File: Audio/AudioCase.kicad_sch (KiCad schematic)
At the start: 3 parts, among them J1 PD給電, J2 入力ジャック, J3 出力ジャック

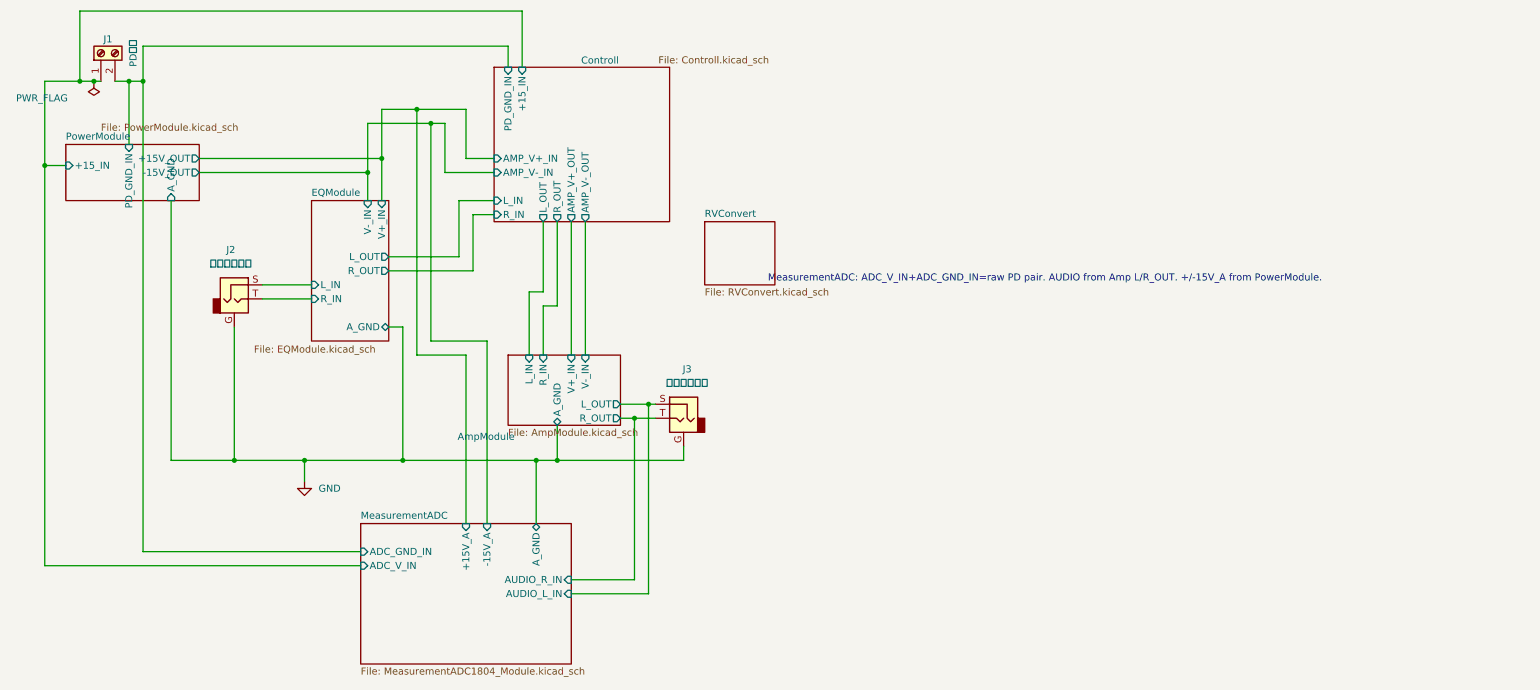
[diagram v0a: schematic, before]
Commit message: Add AdcBuffer unity-gain sheet between Amp and MeasurementADC.
Inserts AdcBufferModule (NE5532/OPA1652 DIP followers, 100k bias, 47Ω
series, 0.1µF decouple) on the parent sheet so Amp AUX remains line-out
while ADC sees a high-Z buffered feed on shared A_GND/±15.

Co-authored-by: m_arino <indare@users.noreply.github.com>
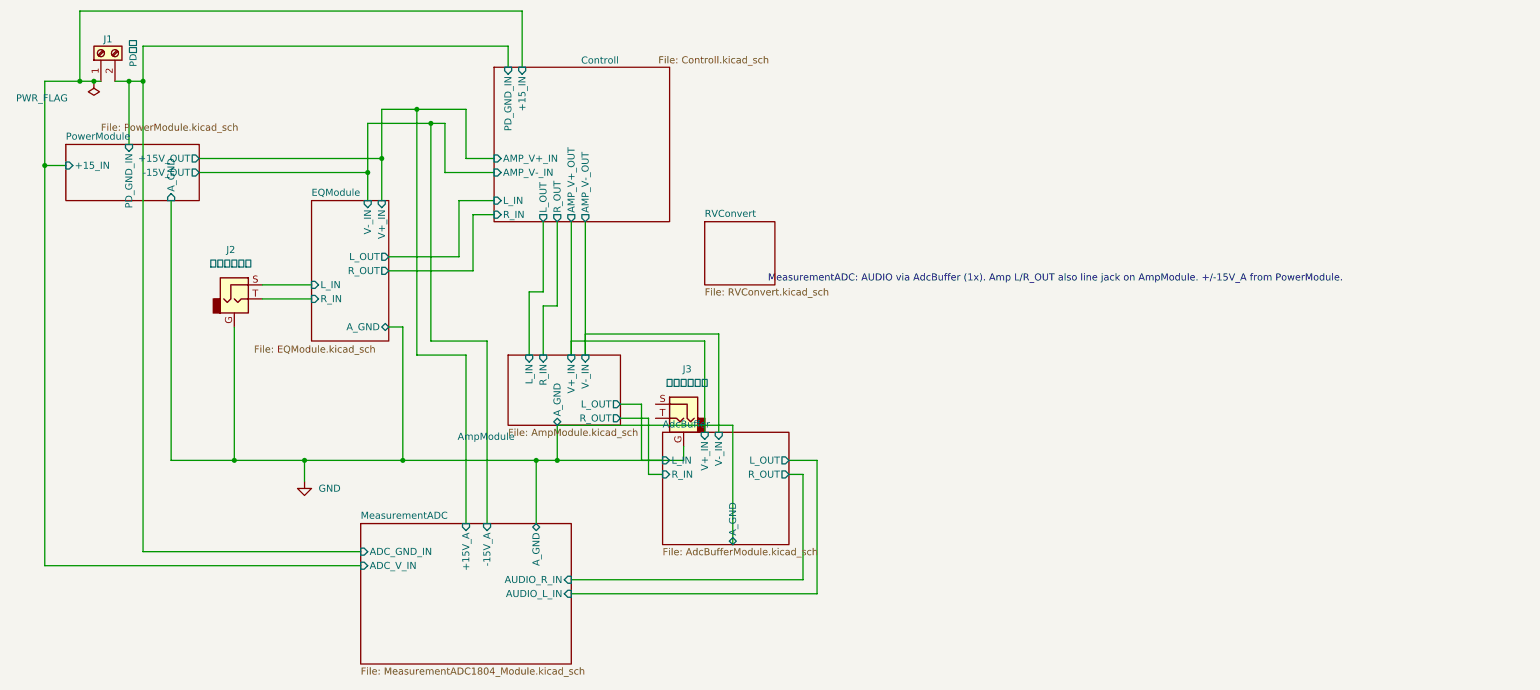
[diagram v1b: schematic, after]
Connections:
- net AmpModule/L_OUT: no longer names the net of J3.S
- net AmpModule/R_OUT: no longer names the net of J3.T
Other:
- added sheet AdcBuffer (AdcBufferModule.kicad_sch)
- note added: "MeasurementADC: AUDIO via AdcBuffer (1x). Amp L/R_OUT also line jack on AmpModule. +/-15V_A from PowerModule."
- note removed: "MeasurementADC: ADC_V_IN+ADC_GND_IN=raw PD pair. AUDIO from Amp L/R_OUT. +/-15V_A from PowerModule."
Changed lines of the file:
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@@
 	(generator_version "10.0")
 	(paper "A4")
-	(text "MeasurementADC: ADC_V_IN+ADC_GND_IN=raw PD pair. AUDIO from Amp L/R_OUT. +/-15V_A from PowerModule."
+	(text "MeasurementADC: AUDIO via AdcBuffer (1x). Amp L/R_OUT also line jack on AmpModule. +/-15V_A from PowerModule."
 		(exclude_from_sim no)
 		(at 156.21 72 0)
@@
 	)
 	(junction
-		(at 134.62 93.98)
-		(diameter 0)
-		(color 0 0 0 0)
-	)
-	(junction
 		(at 90.17 104.14)
 		(diameter 0)
@@
 	)
 	(junction
-		(at 132.08 96.52)
-		(diameter 0)
-		(color 0 0 0 0)
-	)
-	(junction
 		(at 59.69 104.14)
 		(diameter 0)
@@
 	(wire
 		(pts
-			(xy 132.08 96.52) (xy 132.08 125.73)
+			(xy 129.54 93.98) (xy 133.35 93.98)
+		)
+		(stroke
+			(width 0)
+			(type default)
+		)
+	)
+	(wire
+		(pts
+			(xy 133.35 93.98) (xy 133.35 104.14)
+		)
+		(stroke
+			(width 0)
+			(type default)
+		)
+	)
+	(wire
+		(pts
+			(xy 133.35 104.14) (xy 137.16 104.14)
+		)
+		(stroke
+			(width 0)
+			(type default)
+		)
+	)
+	(wire
+		(pts
+			(xy 129.54 96.52) (xy 134.62 96.52)
+		)
+		(stroke
+			(width 0)
+			(type default)
+		)
+	)
+	(wire
+		(pts
+			(xy 134.62 96.52) (xy 134.62 106.68)
+		)
+		(stroke
+			(width 0)
+			(type default)
+		)
+	)
+	(wire
+		(pts
+			(xy 134.62 106.68) (xy 137.16 106.68)
+		)
+		(stroke
+			(width 0)
+			(type default)
+		)
+	)
+	(wire
+		(pts
+			(xy 160.01999999999998 104.14) (xy 165.1 104.14)
+		)
+		(stroke
+			(width 0)
+			(type default)
+		)
+	)
+	(wire
+		(pts
+			(xy 165.1 104.14) (xy 165.1 128.27)
+		)
+		(stroke
+			(width 0)
+			(type default)
+		)
+	)
+	(wire
+		(pts
+			(xy 165.1 128.27) (xy 120.65 128.27)
+		)
+		(stroke
+			(width 0)
+			(type default)
+		)
+	)
+	(wire
+		(pts
+			(xy 160.01999999999998 106.68) (xy 162.56 106.68)
+		)
+		(stroke
+			(width 0)
+			(type default)
+		)
+	)
+	(wire
+		(pts
+			(xy 162.56 106.68) (xy 162.56 125.73)
+		)
+		(stroke
+			(width 0)
+			(type default)
+		)
+	)
+	(wire
+		(pts
+			(xy 162.56 125.73) (xy 120.65 125.73)
+		)
+		(stroke
+			(width 0)
+			(type default)
+		)
+	)
+	(wire
+		(pts
+			(xy 120.65 85.09) (xy 120.65 82.55)
+		)
+		(stroke
+			(width 0)
+			(type default)
+		)
+	)
+	(wire
+		(pts
+			(xy 120.65 82.55) (xy 144.78 82.55)
+		)
+		(stroke
+			(width 0)
+			(type default)
+		)
+	)
+	(wire
+		(pts
+			(xy 144.78 82.55) (xy 144.78 99.06)
+		)
+		(stroke
+			(width 0)
+			(type default)
+		)
+	)
+	(wire
+		(pts
+			(xy 123.19 85.09) (xy 123.19 81.28)
+		)
+		(stroke
+			(width 0)
+			(type default)
+		)
+	)
+	(wire
+		(pts
+			(xy 123.19 81.28) (xy 147.32 81.28)
+		)
+		(stroke
+			(width 0)
+			(type default)
+		)
+	)
+	(wire
+		(pts
+			(xy 147.32 81.28) (xy 147.32 99.06)
+		)
+		(stroke
+			(width 0)
+			(type default)
+		)
+	)
+	(wire
+		(pts
+			(xy 118.11 97.79) (xy 149.85999999999999 97.79)
+		)
+		(stroke
+			(width 0)
+			(type default)
+		)
+	)
+	(wire
+		(pts
+			(xy 149.85999999999999 97.79) (xy 149.85999999999999 119.38)
 		)
 		(stroke
@@
 	(wire
 		(pts
-			(xy 135.89 93.98) (xy 134.62 93.98)
-		)
-		(stroke
-			(width 0)
-			(type default)
-		)
-	)
-	(wire
-		(pts
 			(xy 59.69 80.01) (xy 59.69 104.14)
 		)
@@
 	(wire
 		(pts
-			(xy 132.08 125.73) (xy 120.65 125.73)
-		)
-		(stroke
-			(width 0)
-			(type default)
-		)
-	)
-	(wire
-		(pts
 			(xy 106.68 52.07) (xy 97.79 52.07)
 		)
@@
 	(wire
 		(pts
-			(xy 129.54 96.52) (xy 132.08 96.52)
-		)
-		(stroke
-			(width 0)
-			(type default)
-		)
-	)
-	(wire
-		(pts
 			(xy 118.11 97.79) (xy 118.11 104.14)
 		)
@@
 	(wire
 		(pts
-			(xy 132.08 96.52) (xy 135.89 96.52)
-		)
-		(stroke
-			(width 0)
-			(type default)
-		)
-	)
-	(wire
-		(pts
 			(xy 120.65 60.96) (xy 120.65 85.09)
 		)
@@
 	(wire
 		(pts
-			(xy 134.62 93.98) (xy 129.54 93.98)
-		)
-		(stroke
-			(width 0)
-			(type default)
-		)
-	)
-	(wire
-		(pts
 			(xy 115.57 60.96) (xy 115.57 73.66)
 		)
@@
 	(wire
 		(pts
-			(xy 134.62 93.98) (xy 134.62 128.27)
-		)
-		(stroke
-			(width 0)
-			(type default)
-		)
-	)
-	(wire
-		(pts
 			(xy 100.33 67.31) (xy 100.33 57.15)
 		)
@@
 		(pts
 			(xy 43.18 29.21) (xy 109.22 29.21)
-		)
-		(stroke
-			(width 0)
-			(type default)
-		)
-	)
-	(wire
-		(pts
-			(xy 120.65 128.27) (xy 134.62 128.27)
 		)
 		(stroke
@@
 				)
 			)
+		)
+	)
+	(sheet
+		(at 137.16 99.06)
+		(size 22.86 20.32)
+		(exclude_from_sim no)
+		(in_bom yes)
+		(on_board yes)
+		(dnp no)
+		(stroke
+			(width 0.1524)
+			(type solid)
+		)
+		(fill
+			(color 0 0 0 0)
+		)
+		(property "Sheetname" "AdcBuffer"
+			(at 137.16 98.3484 0)
+			(show_name no)
+			(do_not_autoplace no)
+			(effects
+				(font
+					(size 1.27 1.27)
+				)
+				(justify left bottom)
+			)
+		)
+		(property "Sheetfile" "AdcBufferModule.kicad_sch"
+			(at 137.16 119.96419999999999 0)
+			(show_name no)
+			(do_not_autoplace no)
+			(effects
+				(font
+					(size 1.27 1.27)
+				)
+				(justify left top)
+			)
+		)
+		(pin "L_IN" input
+			(at 137.16 104.14 180)
+			(effects
+				(font
+					(size 1.27 1.27)
+				)
+				(justify left)
+			)
+		)
+		(pin "R_IN" input
+			(at 137.16 106.68 180)
+			(effects
+				(font
+					(size 1.27 1.27)
+				)
+				(justify left)
+			)
+		)
+		(pin "L_OUT" output
+			(at 160.01999999999998 104.14 0)
+			(effects
+				(font
+					(size 1.27 1.27)
+				)
+				(justify right)
+			)
+		)
+		(pin "R_OUT" output
+			(at 160.01999999999998 106.68 0)
+			(effects
+				(font
+					(size 1.27 1.27)
+				)
+				(justify right)
+			)
+		)
+		(pin "V+_IN" input
+			(at 144.78 99.06 90)
+			(effects
+				(font
+					(size 1.27 1.27)
+				)
+				(justify right)
+			)
+		)
+		(pin "V-_IN" input
+			(at 147.32 99.06 90)
+			(effects
+				(font
+					(size 1.27 1.27)
+				)
+				(justify right)
+			)
+		)
+		(pin "A_GND" bidirectional
+			(at 149.85999999999999 119.38 270)
+			(effects
+				(font
+					(size 1.27 1.27)
+				)
+				(justify left)
+			)
+		)
+		(instances
+			(project "AudioCase"
+				(path "/760b9589-09e7-434e-9ca2-6e4136e3b7a2"
+					(page "8")
+				)
+			)
